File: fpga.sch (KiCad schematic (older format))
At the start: 4 parts

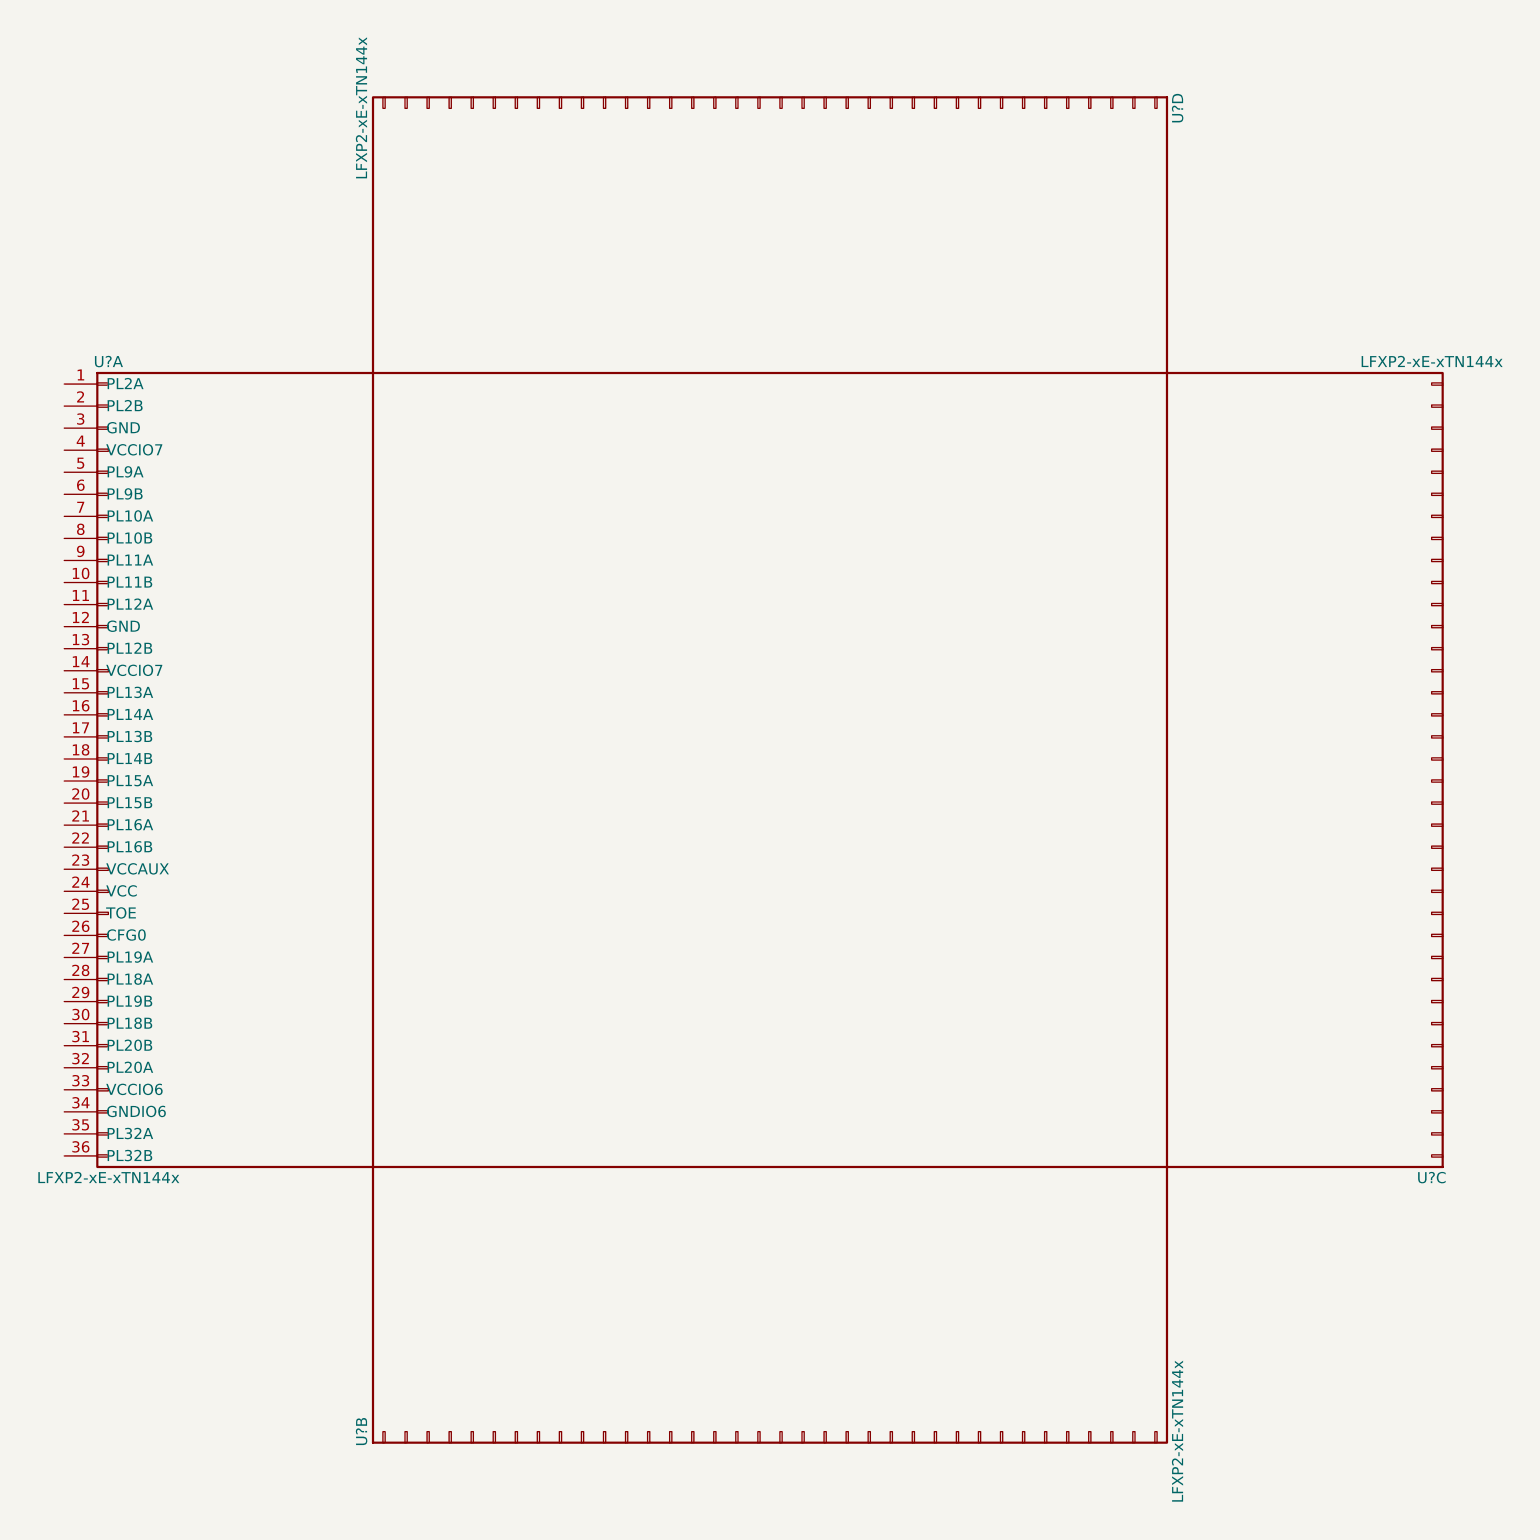
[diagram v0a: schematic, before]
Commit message: schematics: correct audio jack and return of footprint association for fpga chip
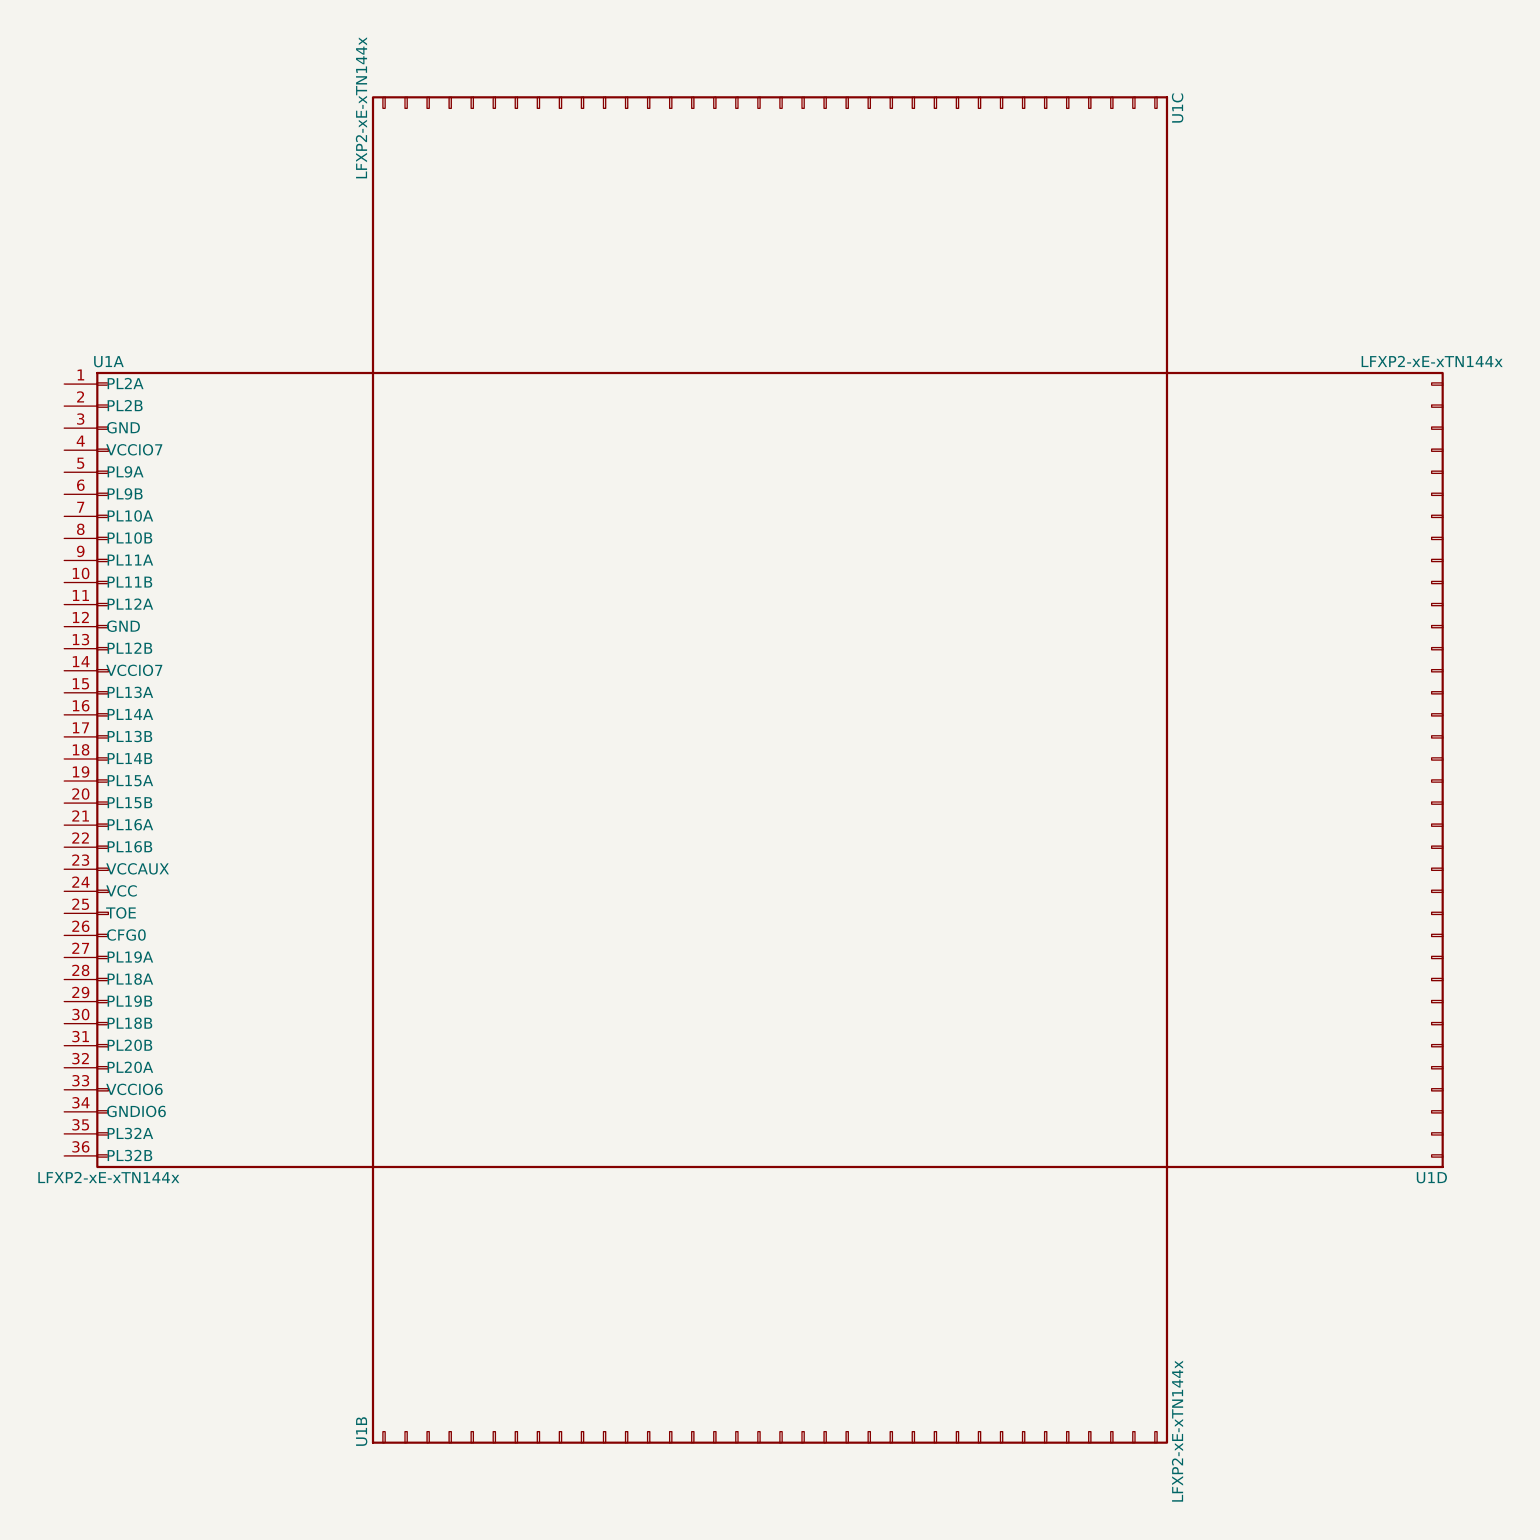
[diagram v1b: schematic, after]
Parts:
- U1: renamed from U?; footprint (none) -> Housings_QFP:TQFP-144_20x20mm_Pitch0.5mm
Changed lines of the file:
@@
 $EndDescr
 $Comp
-L LFXP2-xE-xTN144x U?
+L LFXP2-xE-xTN144x U1
 U 1 1 5A13E2F6
 P 1400 4050
-F 0 "U?" H 1400 5850 50  0000 C CNN
+F 0 "U1" H 1400 5850 50  0000 C CNN
 F 1 "LFXP2-xE-xTN144x" H 1400 2150 50  0000 C CNN
-F 2 "" H 1400 4050 50  0001 C CNN
+F 2 "Housings_QFP:TQFP-144_20x20mm_Pitch0.5mm" H 1400 4050 50  0001 C CNN
 F 3 "" H 1400 4050 50  0001 C CNN
 	1    1400 4050
@@
 $EndComp
 $Comp
-L LFXP2-xE-xTN144x U?
+L LFXP2-xE-xTN144x U1
 U 2 1 5A13E3EB
 P 4350 7100
-F 0 "U?" H 4350 8900 50  0000 C CNN
+F 0 "U1" H 4350 8900 50  0000 C CNN
 F 1 "LFXP2-xE-xTN144x" H 4350 5200 50  0000 C CNN
-F 2 "" H 4350 7100 50  0001 C CNN
+F 2 "Housings_QFP:TQFP-144_20x20mm_Pitch0.5mm" H 4350 7100 50  0001 C CNN
 F 3 "" H 4350 7100 50  0001 C CNN
 	2    4350 7100
@@
 $EndComp
 $Comp
-L LFXP2-xE-xTN144x U?
-U 3 1 5A13E576
+L LFXP2-xE-xTN144x U1
+U 4 1 5A13E576
 P 7400 4150
-F 0 "U?" H 7400 5950 50  0000 C CNN
+F 0 "U1" H 7400 5950 50  0000 C CNN
 F 1 "LFXP2-xE-xTN144x" H 7400 2250 50  0000 C CNN
-F 2 "" H 7400 4150 50  0001 C CNN
+F 2 "Housings_QFP:TQFP-144_20x20mm_Pitch0.5mm" H 7400 4150 50  0001 C CNN
 F 3 "" H 7400 4150 50  0001 C CNN
-	3    7400 4150
+	4    7400 4150
 	-1   0    0    1
 $EndComp
 $Comp
-L LFXP2-xE-xTN144x U?
-U 4 1 5A13E5E5
+L LFXP2-xE-xTN144x U1
+U 3 1 5A13E5E5
 P 4450 1100
-F 0 "U?" H 4450 2900 50  0000 C CNN
+F 0 "U1" H 4450 2900 50  0000 C CNN
 F 1 "LFXP2-xE-xTN144x" H 4450 -800 50  0000 C CNN
-F 2 "" H 4450 1100 50  0001 C CNN
+F 2 "Housings_QFP:TQFP-144_20x20mm_Pitch0.5mm" H 4450 1100 50  0001 C CNN
 F 3 "" H 4450 1100 50  0001 C CNN
-	4    4450 1100
+	3    4450 1100
 	0    1    1    0
 $EndComp
